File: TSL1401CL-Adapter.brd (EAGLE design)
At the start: 39 x 27.9 mm, 3 parts

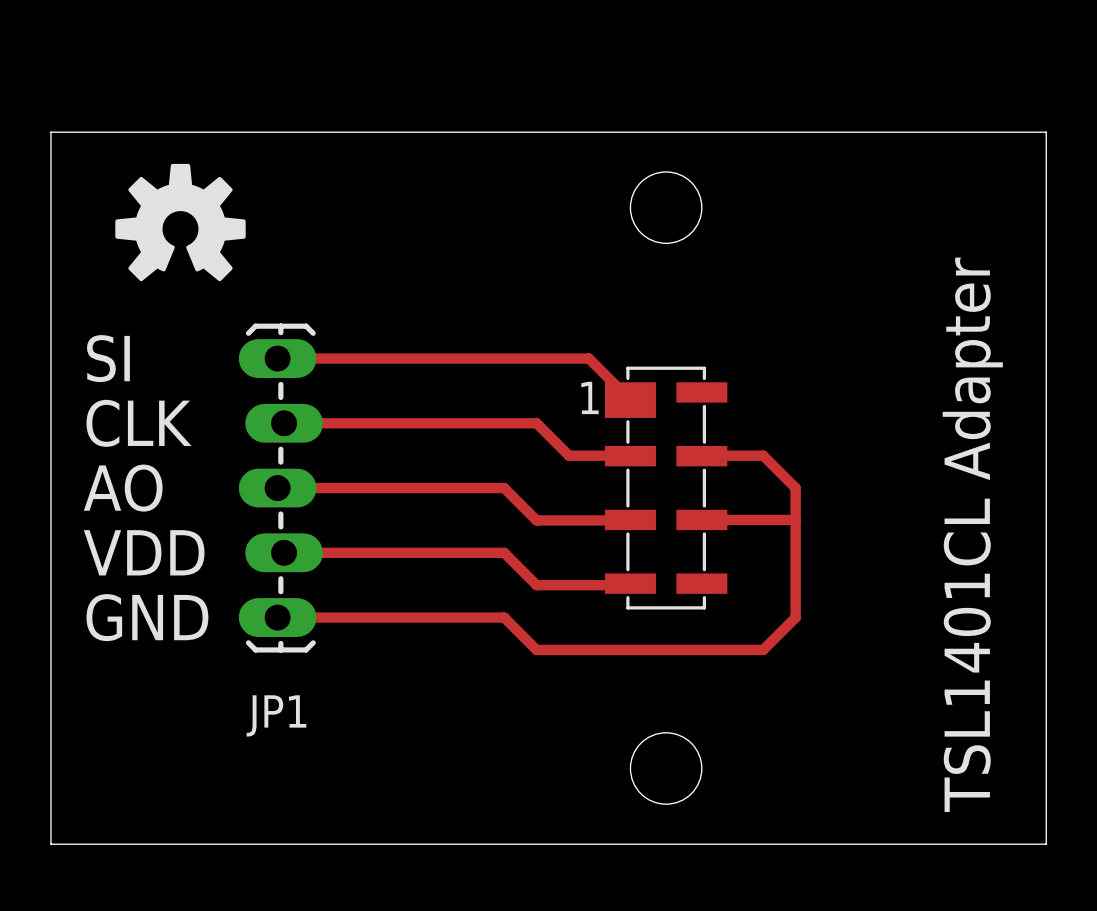
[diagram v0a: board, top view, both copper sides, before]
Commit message: Added 2x3 Shroud and made the board square with drill holes
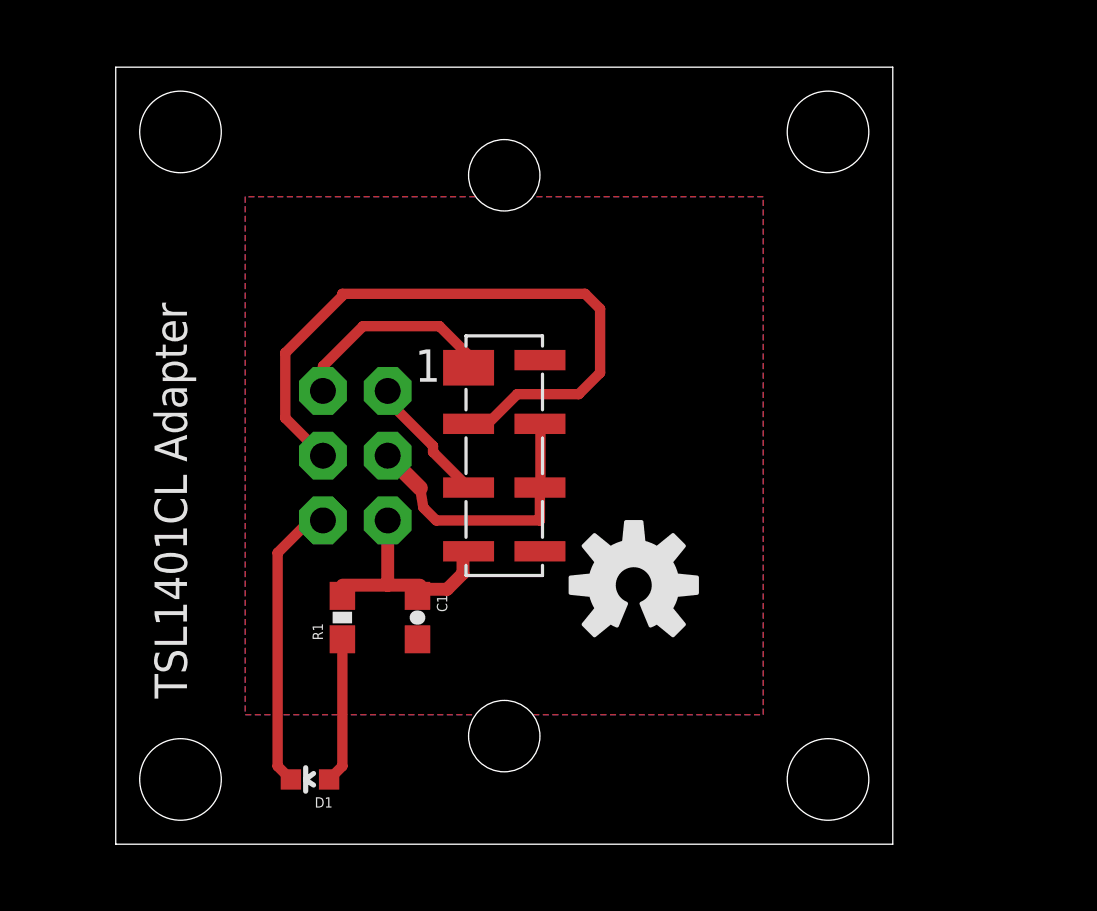
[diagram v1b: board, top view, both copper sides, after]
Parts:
- removed JP1: (no value), SparkFun:1X05_LOCK_LONGPADS
- added C1: 1uF, SparkFun-Passives:0603-CAP
- added D1: GREEN, SparkFun-LED:LED-0603
- added JP2: Sensor, SparkFun-Connectors:2X3-SHROUDED
- added R1: 1K, SparkFun-Resistors:0603-RES
- moved U$2 22.6 mm to (20.3, 10.2)
- moved U$1 6.48 mm to (15.2, 15.2)
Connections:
- new net GND: C1.2, JP2.3, U$1.GND1, U$1.GND2
- new net N$6: D1.C, JP2.6
- net N$1: now also JP2.2; no longer JP1.5
- net N$2: now also JP2.4; no longer JP1.4
- net N$3: now also JP2.1; no longer JP1.3
- net N$4: now also C1.1, JP2.5, R1.2; no longer JP1.2
- net N$5: now also D1.A, R1.1; no longer JP1.1, U$1.GND1, U$1.GND2
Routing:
- net N$5: track 34.4 -> 5.72 mm
- net N$2: track 14.1 -> 26.8 mm
- net N$6: track 0.00 -> 11.4 mm
- net GND: track 0.00 -> 11.2 mm
- net N$3: track 14.4 -> 5.13 mm
- net N$1: track 14.5 -> 8.29 mm
- net N$4: track 14.1 -> 9.34 mm
- added copper zone on layer 1, net GND
- added copper zone on layer 16, net GND
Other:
- board size 39 x 27.9 mm -> 30.5 x 30.5 mm
- board text added: "March 28, 2013"
- board text removed: "AO"
- board text removed: "CLK"
- board text removed: "February 7, 2013"
- board text removed: "GND"
- board text removed: "SI"
- board text removed: "VDD"

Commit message: Modified to be used as a remote sensor to the pgFocus project
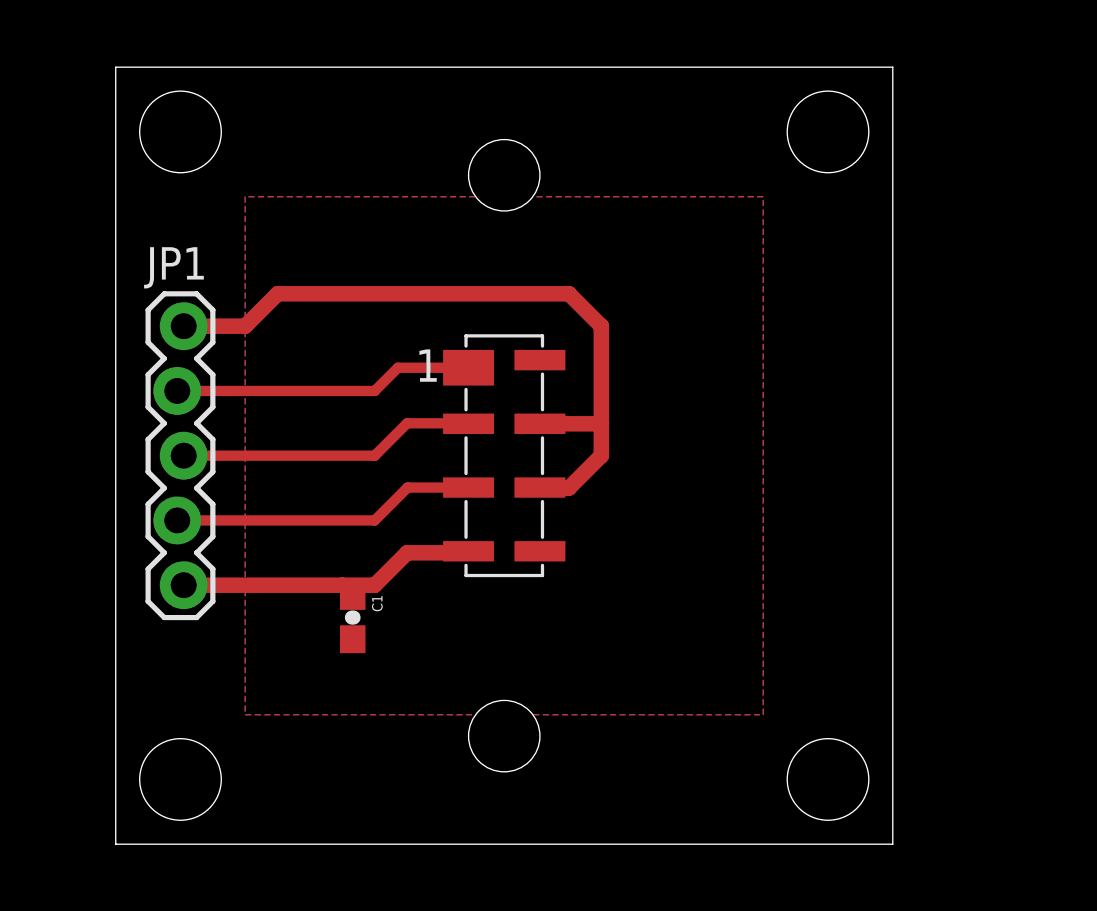
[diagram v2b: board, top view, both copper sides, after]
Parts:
- removed D1: GREEN, SparkFun-LED:LED-0603
- removed JP2: Sensor, SparkFun-Connectors:2X3-SHROUDED
- removed R1: 1K, SparkFun-Resistors:0603-RES
- added JP1: (no value), SparkFun-Connectors:1X05_LOCK
- moved U$2 19.0 mm to (8.89, 25.4), flipped to the bottom
- moved C1 2.54 mm to (9.30, 8.89)
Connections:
- removed net N$1: JP2.2, U$1.SI
- removed net N$2: JP2.4, U$1.CLK
- removed net N$3: JP2.1, U$1.AO
- removed net N$4: C1.1, JP2.5, R1.2, U$1.VDD
- removed net N$5: D1.A, R1.1
- removed net N$6: D1.C, JP2.6
- new net +5V: C1.1, JP1.5, U$1.VDD
- new net AO: JP1.4, U$1.AO
- new net CLK: JP1.3, U$1.CLK
- new net SI: JP1.2, U$1.SI
- net GND: now also JP1.1; no longer JP2.3
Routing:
- net N$2: track 26.8 -> 0.00 mm
- net GND: track 11.2 -> 27.9 mm
- net +5V: track 0.00 -> 12.3 mm
- net AO: track 0.00 -> 12.0 mm
- net SI: track 0.00 -> 11.8 mm
- net CLK: track 0.00 -> 11.7 mm
- net N$6: track 11.4 -> 0.00 mm
- net N$4: track 9.34 -> 0.00 mm
- net N$1: track 8.29 -> 0.00 mm
- net N$5: track 5.72 -> 0.00 mm
- net N$3: track 5.13 -> 0.00 mm
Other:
- board text added: "5V"
- board text added: "AO"
- board text added: "CLK"
- board text added: "GND"
- board text added: "SI"

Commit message: Changed connector to JST 5 Pin
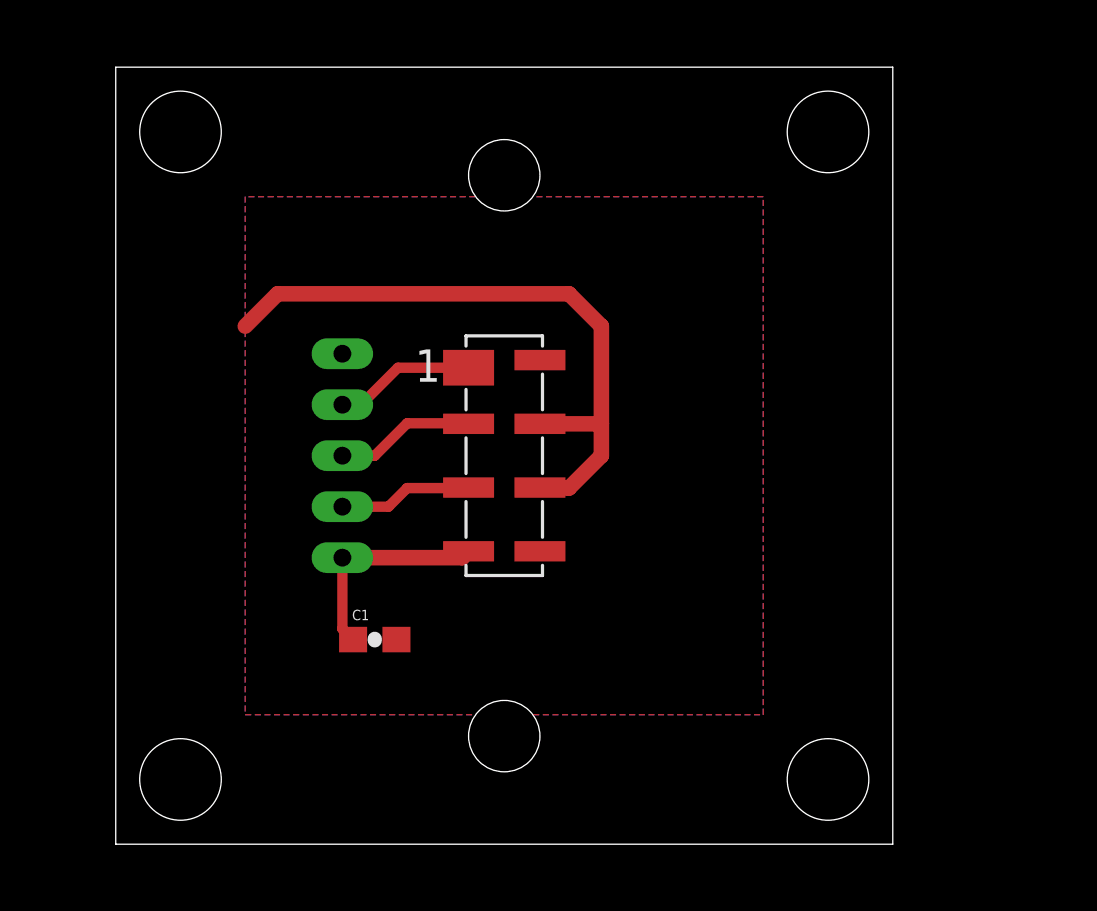
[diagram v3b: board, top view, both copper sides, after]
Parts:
- removed JP1: (no value), SparkFun-Connectors:1X05_LOCK
- added U$3: M05, BIG:M05JST-PTH
- C1: value 1uF -> 1uF (16V)
- moved C1 1.22 mm to (10.2, 8.03), turned to 0 degrees
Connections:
- net +5V: now also U$3.P$5; no longer JP1.5
- net AO: now also U$3.P$4; no longer JP1.4
- net CLK: now also U$3.P$3; no longer JP1.3
- net GND: now also U$3.P$1; no longer JP1.1
- net SI: now also U$3.P$2; no longer JP1.2
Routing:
- net AO: track 12.0 -> 5.26 mm
- net SI: track 11.8 -> 5.55 mm
- net CLK: track 11.7 -> 5.48 mm
- net +5V: track 12.3 -> 8.44 mm
- net GND: track 27.9 -> 25.5 mm
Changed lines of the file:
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@@
 <dimension x1="15.24" y1="15.24" x2="0" y2="15.24" x3="7.62" y3="33.02" layer="51" dtype="vertical"/>
 <dimension x1="15.24" y1="15.24" x2="15.24" y2="30.48" x3="-2.54" y3="22.86" layer="51" dtype="vertical"/>
-<text x="10.795" y="19.304" size="1.778" layer="22" rot="MR0">GND</text>
-<text x="10.795" y="11.684" size="1.778" layer="22" rot="MR0">AO</text>
-<text x="10.795" y="16.764" size="1.778" layer="22" rot="MR0">SI</text>
-<text x="10.795" y="14.224" size="1.778" layer="22" rot="MR0">CLK</text>
-<text x="10.795" y="9.144" size="1.778" layer="22" rot="MR0">5V</text>
+<text x="16.002" y="18.542" size="1.27" layer="22" rot="MR0">GND</text>
+<text x="16.129" y="12.7" size="1.27" layer="22" rot="MR0">AO</text>
+<text x="16.002" y="16.764" size="1.27" layer="22" rot="MR0">SI</text>
+<text x="16.002" y="14.605" size="1.27" layer="22" rot="MR0">CLK</text>
+<text x="16.129" y="10.541" size="1.27" layer="22" rot="MR0">5V</text>
 <dimension x1="15.24" y1="15.24" x2="2.54" y2="27.94" x3="-8.89" y3="21.59" layer="51" dtype="vertical"/>
 <dimension x1="15.24" y1="15.24" x2="27.94" y2="15.24" x3="21.59" y3="-2.54" layer="51" dtype="horizontal"/>
@@
 <element name="U$1" library="BIG" package="TSL1401CL" value="TSL1401CL" x="15.24" y="15.24"/>
 <element name="U$2" library="SparkFun" package="OSHW-LOGO-M" value="OSHW-LOGOM" x="8.89" y="25.4" rot="MR0"/>
-<element name="C1" library="SparkFun-Passives" package="0603-CAP" value="1uF" x="9.2964" y="8.89" rot="R270"/>
-<element name="JP1" library="SparkFun-Connectors" package="1X05_LOCK" value="" x="2.54" y="20.32" smashed="yes" rot="R270">
-<attribute name="NAME" x="1.1938" y="22.1488" size="1.27" layer="25" ratio="10"/>
-<attribute name="VALUE" x="-1.27" y="21.59" size="1.27" layer="27" rot="R270"/>
-</element>
+<element name="C1" library="SparkFun-Passives" package="0603-CAP" value="1uF (16V)" x="10.16" y="8.0264"/>
+<element name="U$3" library="BIG" package="M05JST-PTH" value="M05" x="8.89" y="15.24" rot="MR180"/>
 </elements>
 <signals>
@@
 <contactref element="U$1" pad="VDD"/>
 <contactref element="C1" pad="1"/>
-<contactref element="JP1" pad="5"/>
-<wire x1="13.78" y1="11.43" x2="13.84" y2="11.49" width="0.4064" layer="1"/>
-<wire x1="13.78" y1="11.43" x2="11.43" y2="11.43" width="0.6096" layer="1"/>
-<wire x1="11.43" y1="11.43" x2="10.16" y2="10.16" width="0.6096" layer="1"/>
-<wire x1="10.16" y1="10.16" x2="8.89" y2="10.16" width="0.6096" layer="1"/>
-<wire x1="8.89" y1="10.16" x2="2.667" y2="10.16" width="0.6096" layer="1"/>
-<wire x1="9.2964" y1="9.74" x2="9.2964" y2="9.7536" width="0.4064" layer="1"/>
-<wire x1="9.2964" y1="9.7536" x2="8.89" y2="10.16" width="0.4064" layer="1"/>
+<contactref element="U$3" pad="P$5"/>
+<wire x1="8.89" y1="11.24" x2="13.59" y2="11.24" width="0.6096" layer="1"/>
+<wire x1="13.59" y1="11.24" x2="13.84" y2="11.49" width="0.6096" layer="1"/>
+<wire x1="8.89" y1="11.24" x2="8.89" y2="8.4464" width="0.4064" layer="1"/>
+<wire x1="8.89" y1="8.4464" x2="9.31" y2="8.0264" width="0.4064" layer="1"/>
 </signal>
 <signal name="GND">
@@
 <wire x1="16.66" y1="14.01" x2="16.64" y2="13.99" width="0.4064" layer="1"/>
 <wire x1="16.637" y1="13.987" x2="16.64" y2="13.99" width="0.4064" layer="1"/>
-<contactref element="JP1" pad="1"/>
-<wire x1="2.667" y1="20.32" x2="5.08" y2="20.32" width="0.6096" layer="1"/>
 <wire x1="5.08" y1="20.32" x2="6.35" y2="21.59" width="0.6096" layer="1"/>
 <wire x1="6.35" y1="21.59" x2="17.78" y2="21.59" width="0.6096" layer="1"/>
@@
 <wire x1="16.64" y1="16.49" x2="19.03" y2="16.49" width="0.6096" layer="1"/>
 <wire x1="19.03" y1="16.49" x2="19.05" y2="16.51" width="0.6096" layer="1"/>
+<contactref element="U$3" pad="P$1"/>
 </signal>
 <signal name="SI">
 <contactref element="U$1" pad="SI"/>
-<contactref element="JP1" pad="2"/>
-<wire x1="2.413" y1="17.78" x2="10.16" y2="17.78" width="0.4064" layer="1"/>
-<wire x1="13.84" y1="18.69" x2="11.07" y2="18.69" width="0.4064" layer="1"/>
-<wire x1="11.07" y1="18.69" x2="10.16" y2="17.78" width="0.4064" layer="1"/>
+<contactref element="U$3" pad="P$2"/>
+<wire x1="9.62" y1="17.24" x2="8.89" y2="17.24" width="0.4064" layer="1"/>
+<wire x1="9.62" y1="17.24" x2="11.07" y2="18.69" width="0.4064" layer="1"/>
+<wire x1="11.07" y1="18.69" x2="13.84" y2="18.69" width="0.4064" layer="1"/>
 </signal>
 <signal name="AO">
 <contactref element="U$1" pad="AO"/>
-<contactref element="JP1" pad="4"/>
-<wire x1="13.84" y1="13.99" x2="11.45" y2="13.99" width="0.4064" layer="1"/>
-<wire x1="11.45" y1="13.99" x2="10.16" y2="12.7" width="0.4064" layer="1"/>
-<wire x1="10.16" y1="12.7" x2="2.413" y2="12.7" width="0.4064" layer="1"/>
+<wire x1="11.43" y1="13.97" x2="13.82" y2="13.97" width="0.4064" layer="1"/>
+<wire x1="13.82" y1="13.97" x2="13.84" y2="13.99" width="0.4064" layer="1"/>
+<contactref element="U$3" pad="P$4"/>
+<wire x1="10.7" y1="13.24" x2="11.43" y2="13.97" width="0.4064" layer="1"/>
+<wire x1="10.7" y1="13.24" x2="8.89" y2="13.24" width="0.4064" layer="1"/>
 </signal>
 <signal name="CLK">
 <contactref element="U$1" pad="CLK"/>
-<contactref element="JP1" pad="3"/>
-<wire x1="2.667" y1="15.24" x2="10.16" y2="15.24" width="0.4064" layer="1"/>
+<contactref element="U$3" pad="P$3"/>
+<wire x1="8.89" y1="15.24" x2="10.16" y2="15.24" width="0.4064" layer="1"/>
 <wire x1="10.16" y1="15.24" x2="11.43" y2="16.51" width="0.4064" layer="1"/>
 <wire x1="11.43" y1="16.51" x2="13.82" y2="16.51" width="0.4064" layer="1"/>
